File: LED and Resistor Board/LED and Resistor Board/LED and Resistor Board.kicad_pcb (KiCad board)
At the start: 2 copper layers, 3 parts, among them J1 Barrel_Jack_MountingPin

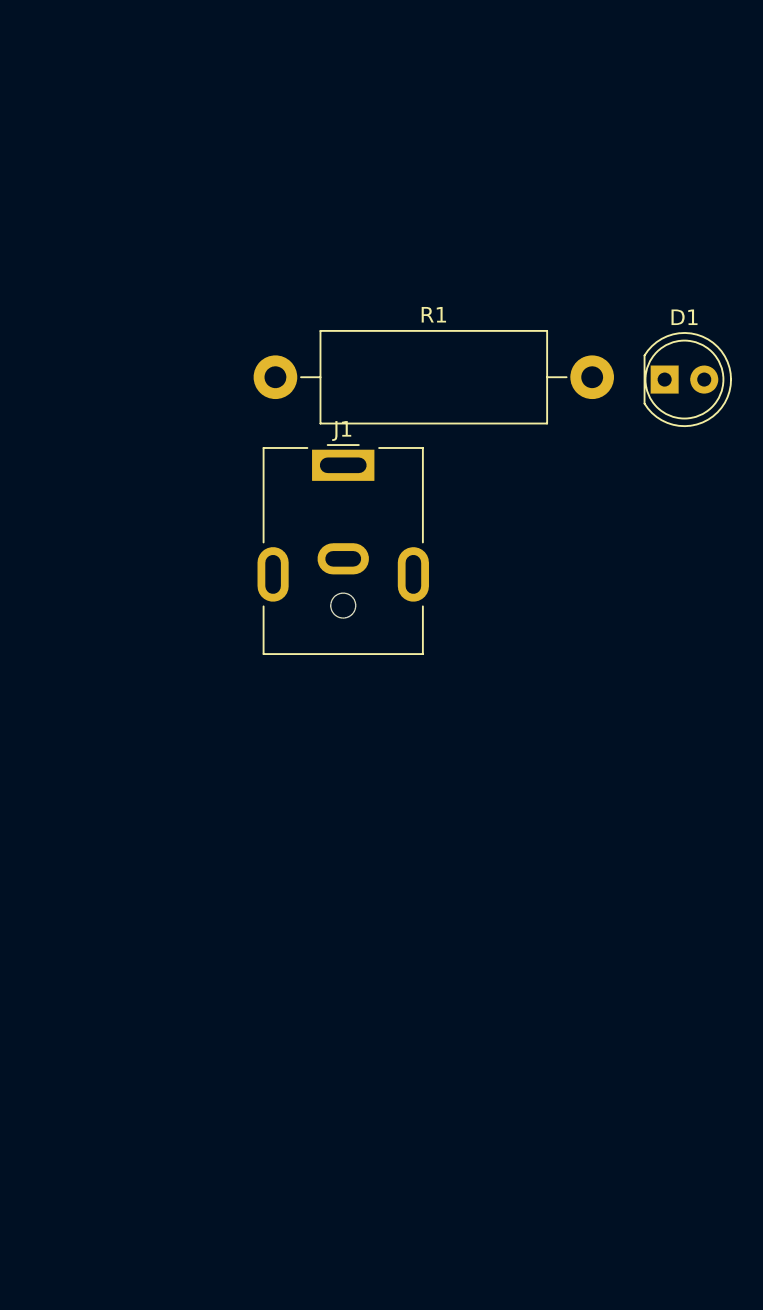
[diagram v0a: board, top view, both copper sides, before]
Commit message: Added silkscreen detail
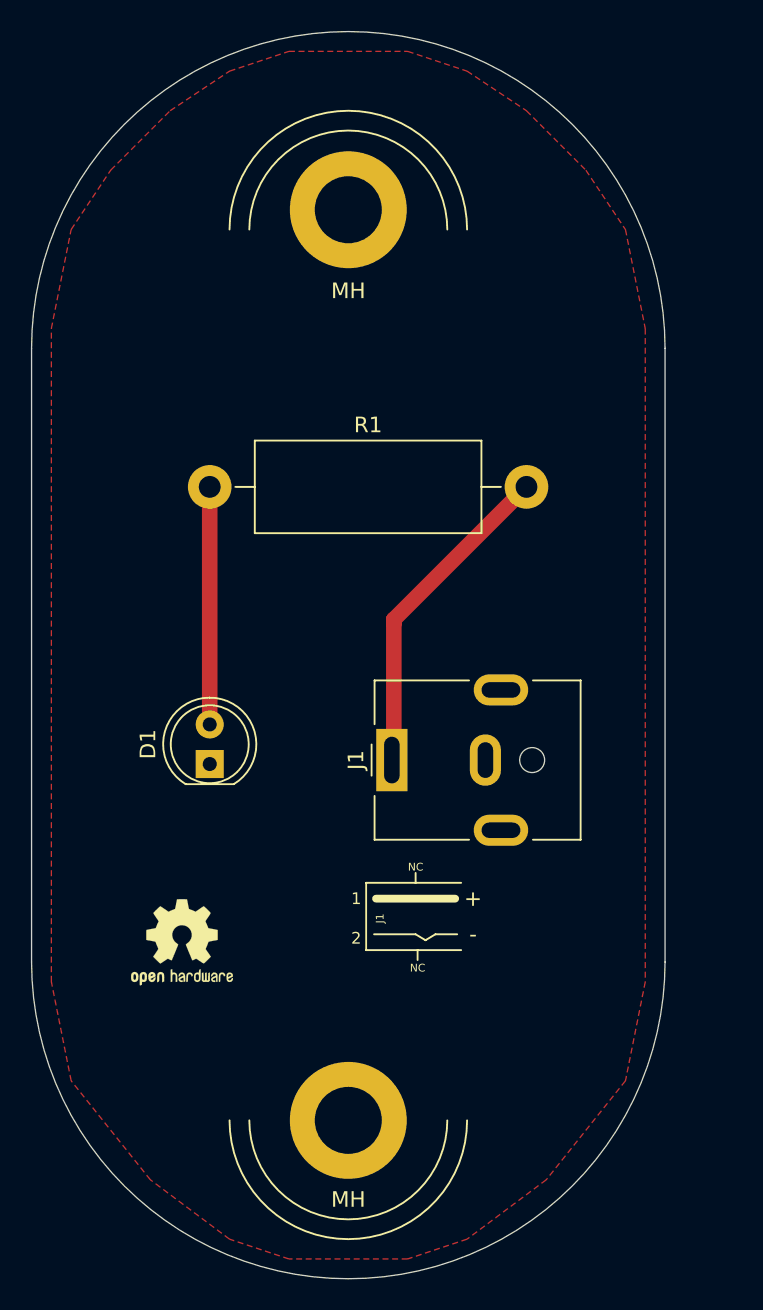
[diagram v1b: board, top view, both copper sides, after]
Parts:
- added MH: MountingHole_4.3mm_M4_DIN965_Pad, MountingHole:MountingHole_4.3mm_M4_DIN965_Pad, F.Cu at (134.6, 80.0)
- added MH: MountingHole_4.3mm_M4_DIN965_Pad, MountingHole:MountingHole_4.3mm_M4_DIN965_Pad, F.Cu at (134.6, 138.4)
- added REF**: KiCad-Logo2_6mm_SilkScreen, Symbol:KiCad-Logo2_6mm_SilkScreen, B.Cu at (142.0, 126.6)
- added REF**: OSHW-Logo2_7.3x6mm_SilkScreen, Symbol:OSHW-Logo2_7.3x6mm_SilkScreen, F.Cu at (124.0, 127.0)
- added REF**: RoHS-Logo_6mm_SilkScreen, Symbol:RoHS-Logo_6mm_SilkScreen, B.Cu at (139.6, 104.8)
- moved D1 38.2 mm to (125.7, 115.6), turned to 90 degrees
- moved J1 19.2 mm to (137.4, 115.3), turned to 90 degrees
- moved R1 8.20 mm to (125.7, 97.8)
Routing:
- net +5V: track 0.00 -> 30.0 mm
- net Net-(D1-Pad2): track 0.00 -> 15.2 mm
- added copper zone on F.Cu, net GND
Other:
- board outline added: 40.6 x 80 mm
- board text added: "+"
- board text added: "-"
- board text added: "1"
- board text added: "2"
- board text added: "J1"
- board text added: "NC"
- board text added: "Udemy KiCad 2nd Edition LED & Resistor Version 1"
